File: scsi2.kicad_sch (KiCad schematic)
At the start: 0 parts

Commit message: Place CPLD, NCR and last 543 (Latched Trabceiver)
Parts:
- added U4: NCR53c710 SCSI Host Controller, Package_QFP:PQFP-160_28x28mm_P0.65mm, symbol NCRSCSI:NCR53c710

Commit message: Update design
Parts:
- added FB1: FerriteBead_Small, symbol Device:FerriteBead_Small
- added J3: TO-LED, Connector_PinHeader_2.54mm:PinHeader_1x03_P2.54mm_Vertical, symbol Connector:Conn_01x03_Pin
- added J4: TO-MB, Connector_PinHeader_2.54mm:PinHeader_1x03_P2.54mm_Vertical, symbol Connector:Conn_01x03_Pin
- added R1, R2, R3: 1K, symbol Device:R
- added R10, R6, R7, R8: 1K, YC324-FK-071KL:RESCAXS127P508X320X70-8N, symbol YC324-FK-071KL:YC324-FK-071KL
- added R11, R9: 120, Resistor_SMD:R_0603_1608Metric, symbol Device:R_Small
- added U7: SST39SF010, Package_SO:TSSOP-32_8x11mm_P0.65mm, symbol 39SF010-TSOP:SST39SF010
- added Y1: Abracon ACO-50MHz, Oscillator:Oscillator_DIP-14, symbol Oscillator:ACO-xxxMHz
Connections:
- net GND: now reaches U4.109 (V_{SS})
- net GND: now also U4.113 (V_{SS}), U4.118 (V_{SS}), U4.123 (V_{SS}), U4.128 (V_{SS}), U4.136 (V_{SS}), U4.143 (V_{SS}), U4.149 (V_{SS}), U4.15 (V_{SS}), U4.156 (V_{SS}), U4.2 (V_{SS}), U4.22 (V_{SS}), U4.31 (V_{SS}), U4.46 (V_{SS}), U4.54 (V_{SS}), U4.61 (V_{SS}), U4.69 (V_{SS}), U4.75 (V_{SS}), U4.82 (V_{SS}), U4.9 (V_{SS}), U4.96 (V_{SS}), U7.24 (GND), U7.30 (CE), Y1.7 (GND)
- net V5: now reaches U4.139 (V_{DD})
- net V5: now also U4.153 (V_{DD}), U4.19 (V_{DD}), U4.39 (V_{DD}), U4.40 (~{HALT}/~{TIP}), U4.49 (V_{DD}), U4.6 (V_{DD}), U4.64 (V_{DD}), U4.79 (V_{DD}), U4.90 (~{BIG_LIT}), U4.91 (BS), U4.95 (~{BOFF}), U4.99 (V_{DD}), J3.2 (Pin_2), J4.2 (Pin_2), R1.1, R10.5, R10.6, R10.7, R10.8, R2.1, R3.1, R6.5, R6.6, R6.7, R6.8, R7.6, R7.7, R7.8, R8.5, R8.6, R8.7, R8.8, U7.8 (VCC), Y1.14 (Vcc)
- net A14: now reaches U4.1 (A14)
- net A14: now also U7.12 (A12)
- net A20: now reaches U4.10 (A20)
- net A20: now also U7.9 (NC)
- net CLK_50M: now reaches U4.102 (SCLK)
- net CLK_50M: now also R11.2
- net NCR_INT: now reaches U4.105 (~{IRQ0})
- net A21: now reaches U4.11 (A21)
- net SCTRL_IO: now reaches U4.110 (I/O)
- net SCTRL_REQ: now reaches U4.111 (~{REQ})
- net SCTRL_CD: now reaches U4.112 (C/D)
- net SCTRL_SEL: now reaches U4.114 (~{SEL})
- net SCTRL_MSG: now reaches U4.115 (~{MSG})
- net SCTRL_RST: now reaches U4.116 (~{RST})
- net SCTRL_ACK: now reaches U4.117 (~{ACK})
- net SCTRL_BSY: now reaches U4.119 (~{BSY})
- net A22: now reaches U4.12 (A22)
- net SCTRL_ATN: now reaches U4.120 (~{ATN})
- net SCDATP: now reaches U4.121 (~{SDP})
- net SCDAT7: now reaches U4.122 (~{SD7})
- net SCDAT6: now reaches U4.124 (~{SD6})
- net SCDAT5: now reaches U4.125 (~{SD5})
- net SCDAT4: now reaches U4.126 (~{SD4})
- net SCDAT3: now reaches U4.127 (~{SD3})
- net SCDAT2: now reaches U4.129 (~{SD2})
- net A23: now reaches U4.13 (A23)
- net SCDAT1: now reaches U4.130 (~{SD1})
- net SCDAT0: now reaches U4.131 (~{SD0})
- net A24: now reaches U4.14 (A24)
- net A0: now reaches U4.144 (A0)
- net A0: now also R8.4
- net A1: now reaches U4.145 (A1)
- net A1: now also R8.3
- net A2: now reaches U4.146 (A2)
- net A2: now also R8.2, U7.20 (A0)
- net A3: now reaches U4.147 (A3)
- net A3: now also R8.1, U7.19 (A1)
- net A4: now reaches U4.148 (A4)
- net A4: now also U7.18 (A2)
- net A5: now reaches U4.150 (A5)
- net A5: now also U7.17 (A3)
- net A6: now reaches U4.151 (A6)
- net A6: now also U7.16 (A4)
- net A7: now reaches U4.152 (A7)
- net A7: now also U7.15 (A5)
- net A8: now reaches U4.154 (A8)
- net A8: now also U7.14 (A6)
- net A9: now reaches U4.155 (A9)
- net A9: now also U7.13 (A7)
- net A10: now reaches U4.157 (A10)
- net A10: now also U7.3 (A8)
- net A11: now reaches U4.158 (A11)
- net A11: now also U7.2 (A9)
- net A12: now reaches U4.159 (A12)
- net A12: now also U7.31 (A10)
- net A25: now reaches U4.16 (A25)
- net A13: now reaches U4.160 (A13)
- net A13: now also U7.1 (A11)
- net A26: now reaches U4.17 (A26)
- net A27: now reaches U4.18 (A27)
- net A28: now reaches U4.20 (A28)
- net A29: now reaches U4.21 (A29)
- net A30: now reaches U4.23 (A30)
- net A31: now reaches U4.24 (A31)
- net PLD_AS: now reaches U4.25 (~{AS}/~{TS})
- net PLD_AS: now also R7.3
- net PLD_SIZ1: now reaches U4.26 (SIZ1)
- net PLD_SIZ1: now also R7.2
- net PLD_SIZ0: now reaches U4.27 (SIZ0)
- net PLD_SIZ0: now also R7.1
- net PLD_FC2: now reaches U4.28 (FCS2/TM2)
- net PLD_FC1: now reaches U4.29 (FCS1/TM1)
- net A15: now reaches U4.3 (A15)
- net A15: now also U7.4 (A13)
- net PLD_FC0: now reaches U4.30 (FCS0/TM0)
- net PLD_READ: now reaches U4.32 (R_W)
- net CBREQ: now reaches U4.33 (~{CBREQ}/~{TT1})
- net CBREQ: now also R6.4
- net CBACK: now reaches U4.35 (~{CBACK}/~{TBI})
- net CBACK: now also R6.3
- net STERM: now reaches U4.36 (STERM/~{TA})
- net STERM: now also R6.2
- net BERR: now reaches U4.37 (~{BERR}/~{TEA})
- net BERR: now also R6.1
- net MASTER: now reaches U4.38 (~{MASTER})
- net A16: now reaches U4.4 (A16)
- net A16: now also U7.5 (A14)
- net CLK: now reaches U4.41 (BCLK)
- net D31: now reaches U4.42 (D31)
- net D31: now also U7.29 (D7)
- net D30: now reaches U4.43 (D30)
- net D30: now also U7.28 (D6)
- net D29: now reaches U4.44 (D29)
- net D29: now also U7.27 (D5)
- net D28: now reaches U4.45 (D28)
- net D28: now also U7.26 (D4)
- net D27: now reaches U4.47 (D27)
- net D26: now reaches U4.48 (D26)
- net A17: now reaches U4.5 (A17)
- net A17: now also U7.11 (A15)
- net D25: now reaches U4.50 (D25)
- net D24: now reaches U4.51 (D24)
- net DP3_ABRT: now reaches U4.52 (DP3/~{ABRT})
- net DP3_ABRT: now also R10.1
- net D23: now reaches U4.53 (D23)
- net D22: now reaches U4.55 (D22)
- net D21: now reaches U4.56 (D21)
- net D20: now reaches U4.57 (D20)
- net D19: now reaches U4.58 (D19)
- net D18: now reaches U4.59 (D18)
- net D17: now reaches U4.60 (D17)
- net D16: now reaches U4.62 (D16)
- net at U4.63 (DP2): now also R3.2
- net D15: now reaches U4.65 (D15)
- net D15: now also U7.25 (D3)
- net D14: now reaches U4.66 (D14)
- net D14: now also U7.23 (D2)
- net D13: now reaches U4.67 (D13)
- net D13: now also U7.22 (D1)
- net D12: now reaches U4.68 (D12)
- net D12: now also U7.21 (D0)
- net A18: now reaches U4.7 (A18)
- net A18: now also U7.10 (A16)
- net D11: now reaches U4.70 (D11)
- net D10: now reaches U4.71 (D10)
- net D9: now reaches U4.72 (D9)
- net D8: now reaches U4.73 (D8)
- net at U4.74 (DP1): now also R2.2
- net D7: now reaches U4.76 (D7)
- net D6: now reaches U4.77 (D6)
- net D5: now reaches U4.78 (D5)
- net A19: now reaches U4.8 (A19)
- net A19: now also U7.6 (NC)
- net D4: now reaches U4.80 (D4)
- net D3: now reaches U4.81 (D3)
- net D2: now reaches U4.83 (D2)
- net D1: now reaches U4.84 (D1)
- net D0: now reaches U4.85 (D0)
- net at U4.86 (DP0): now also R1.2
- net PLD_DS: now reaches U4.87 (~{DS}/DLE)
- net PLD_DS: now also R10.2
- net SLACK: now reaches U4.92 (~{SLACK})
- net SREG: now reaches U4.93 (~{CS})
- new net: R11.1, Y1.8 (OUT)
- new net BGACK: R10.4
- new net IORST: R10.3
- new net LED: R9.1
- new net LEDR: J3.1 (Pin_1), J3.3 (Pin_3), J4.1 (Pin_1), J4.3 (Pin_3), R9.2
- new net ROM_OE: U7.32 (OE)
- new net ROM_WE: U7.7 (PGM)
- no-connect marks 0 -> 18

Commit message: More work. Getting there.
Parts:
- removed R1, R2, R3: 1K, symbol Device:R
- added C34, C36, C38, C40, C42: 0.1uF, symbol Device:C_Small
- added C35, C37, C39, C41: 10uF, symbol Device:C_Small
- added R17: 1K, YC324-FK-071KL:RESCAXS127P508X320X70-8N, symbol YC324-FK-071KL:YC324-FK-071KL
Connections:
- net BGACK: now also R10.3; no longer R10.4
- net DP3_ABRT: now also R17.4; no longer R10.1
- net GND: now also C34.2, C35.2, C36.2, C37.2, C38.2, C39.2, C40.2, C41.2, C42.2
- net IORST: now also R10.2; no longer R10.3
- net PLD_DS: now also R10.1; no longer R10.2
- net SLACK: now also U4.94 (~{RESET}); no longer U4.92 (~{SLACK})
- net SREG: now also U4.95 (~{BOFF}); no longer U4.93 (~{CS})
- net V5: now also U4.92 (~{SLACK}), U4.93 (~{CS}), U4.97 (~{FETCH}), C34.1, C35.1, C36.1, C37.1, C38.1, C39.1, C40.1, C41.1, C42.1, R17.5, R17.6, R17.7, R17.8; no longer R10.5, U4.90 (~{BIG_LIT}), U4.91 (BS), U4.95 (~{BOFF})
- net DP1: now reaches U4.74 (DP1)
- net DP1: now also R17.2
- net DP0: now reaches U4.86 (DP0)
- net DP0: now also R17.1
- net DP2: now reaches U4.63 (DP2)
- net DP2: now also R17.3
- no-connect marks 18 -> 22
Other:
- note added: "P136 <-> P139"
- note added: "P15 <-> P19"
- note added: "P153 <-> P156"
- note added: "P2 <-> P6"
- note added: "P31 <-> P39"
- note added: "P49 <-> P54"
- note added: "P64 <-> P69"
- note added: "P75 <-> P79"
- note added: "P96 <-> P99"
- moved on the sheet: FB1, J3, J4, R10, R6, R7, R8, R9, U7

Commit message: Latest updates
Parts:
- added C32: 10nF, Capacitor_SMD:C_0603_1608Metric_Pad1.08x0.95mm_HandSolder, symbol Device:C_Small
- added FB2, FB3: 60, Capacitor_SMD:C_0603_1608Metric_Pad1.08x0.95mm_HandSolder, symbol Device:FerriteBead_Small
- added R1, R2: 22, Resistor_SMD:R_0603_1608Metric_Pad0.98x0.95mm_HandSolder, symbol Device:R_Small
- added U15: 74ABT74, Package_SO:TSSOP-14_4.4x5mm_P0.65mm, symbol NCRSCSI:74ABT74
- C34, C36, C38, C40, C42: value 0.1uF -> 100nF; footprint (none) -> Capacitor_SMD:C_0603_1608Metric_Pad1.08x0.95mm_HandSolder
- C35, C37, C39, C41: value 10uF -> 10nF; footprint (none) -> Capacitor_SMD:C_0603_1608Metric_Pad1.08x0.95mm_HandSolder
- FB1: value FerriteBead_Small -> 60; footprint (none) -> Capacitor_SMD:C_0603_1608Metric_Pad1.08x0.95mm_HandSolder
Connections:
- net BGACK: now also U4.98 (~{BGACK}/~{BB})
- net CLK: now also R2.1
- net CLK_50M: now also U15.3 (C)
- net GND: now also C32.1, U15.7 (GND)
- net IORST: now also U4.94 (~{RESET})
- net MASTER: now also FB3.2; no longer U4.38 (~{MASTER})
- net PLD_READ: now also FB2.2; no longer U4.32 (R_W)
- net SLACK: now also U4.92 (~{SLACK}); no longer U4.94 (~{RESET})
- net SREG: now also U4.93 (~{CS}); no longer U4.95 (~{BOFF})
- net V5: now also U4.90 (~{BIG_LIT}), U4.91 (BS), U4.95 (~{BOFF}), C32.2, U15.1 (~{R}), U15.10 (~{S}), U15.11 (C), U15.12 (D), U15.13 (~{R}), U15.14 (VCC), U15.4 (~{S}); no longer U4.92 (~{SLACK}), U4.93 (~{CS})
- net at FB1.1: now also U4.101 (~{BR})
- net SBR: now reaches FB1.2
- net SBG: now reaches U4.100 (~{BG})
- new net: R2.2, U15.5 (Q)
- new net: R1.2, U15.6 (~{Q})
- new net: FB2.1, U4.32 (R_W)
- new net: FB3.1, U4.38 (~{MASTER})
- new net CLKI: R1.1, U15.2 (D)
- no-connect marks 22 -> 23
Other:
- moved on the sheet: FB1, R11, Y1

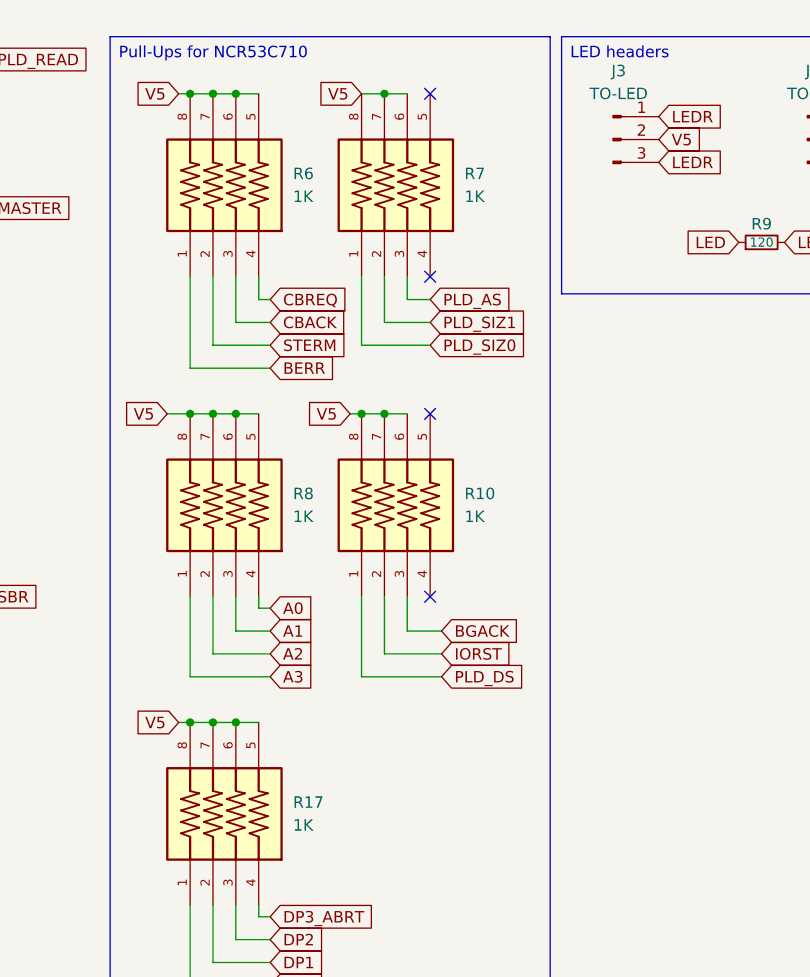
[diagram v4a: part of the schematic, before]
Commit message: Update RN footprint to CAY16_102J4LF
- Rename RNs from R to RN.
- Fix U5 footprint
- Rename pages to be consecutive numbers
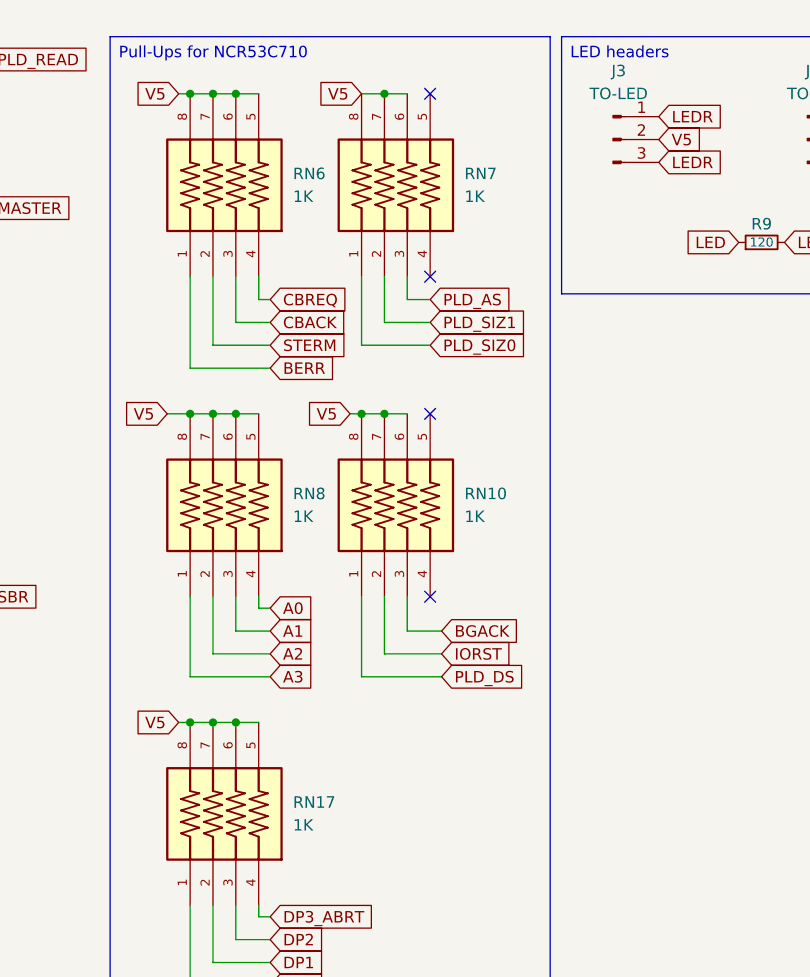
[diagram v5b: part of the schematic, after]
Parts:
- RN10: renamed from R10; footprint YC324-FK-071KL:RESCAXS127P508X320X70-8N -> CAY16_102J4LF:BO_CAY16
- RN17: renamed from R17; footprint YC324-FK-071KL:RESCAXS127P508X320X70-8N -> CAY16_102J4LF:BO_CAY16
- RN6: renamed from R6; footprint YC324-FK-071KL:RESCAXS127P508X320X70-8N -> CAY16_102J4LF:BO_CAY16
- RN7: renamed from R7; footprint YC324-FK-071KL:RESCAXS127P508X320X70-8N -> CAY16_102J4LF:BO_CAY16
- RN8: renamed from R8; footprint YC324-FK-071KL:RESCAXS127P508X320X70-8N -> CAY16_102J4LF:BO_CAY16
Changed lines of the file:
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@@
 		(dnp no)
 		(fields_autoplaced yes)
-		(property "Reference" "R6"
+		(property "Reference" "RN6"
 			(at 135.89 101.5999 90)
 			(effects
@@
 			)
 		)
-		(property "Footprint" "YC324-FK-071KL:RESCAXS127P508X320X70-8N"
+		(property "Footprint" "CAY16_102J4LF:BO_CAY16"
 			(at 129.54 102.87 0)
 			(effects
@@
 			(project ""
 				(path "/8f9f4021-47aa-41d9-bea7-f6ccf72098bb/2daf4fe3-1e72-4ad5-914a-264df02f69b3"
-					(reference "R6")
+					(reference "RN6")
 					(unit 1)
 				)
@@
 		(dnp no)
 		(fields_autoplaced yes)
-		(property "Reference" "R10"
+		(property "Reference" "RN10"
 			(at 154.94 137.1599 90)
 			(effects
@@
 			)
 		)
-		(property "Footprint" "YC324-FK-071KL:RESCAXS127P508X320X70-8N"
+		(property "Footprint" "CAY16_102J4LF:BO_CAY16"
 			(at 148.59 138.43 0)
 			(effects
@@
 			(project ""
 				(path "/8f9f4021-47aa-41d9-bea7-f6ccf72098bb/2daf4fe3-1e72-4ad5-914a-264df02f69b3"
-					(reference "R10")
+					(reference "RN10")
 					(unit 1)
 				)
@@
 		(dnp no)
 		(fields_autoplaced yes)
-		(property "Reference" "R7"
+		(property "Reference" "RN7"
 			(at 154.94 101.5999 90)
 			(effects
@@
 			)
 		)
-		(property "Footprint" "YC324-FK-071KL:RESCAXS127P508X320X70-8N"
+		(property "Footprint" "CAY16_102J4LF:BO_CAY16"
 			(at 148.59 102.87 0)
 			(effects
@@
 			(project ""
 				(path "/8f9f4021-47aa-41d9-bea7-f6ccf72098bb/2daf4fe3-1e72-4ad5-914a-264df02f69b3"
-					(reference "R7")
+					(reference "RN7")
 					(unit 1)
 				)
@@
 		(dnp no)
 		(fields_autoplaced yes)
-		(property "Reference" "R8"
+		(property "Reference" "RN8"
 			(at 135.89 137.1599 90)
 			(effects
@@
 			)
 		)
-		(property "Footprint" "YC324-FK-071KL:RESCAXS127P508X320X70-8N"
+		(property "Footprint" "CAY16_102J4LF:BO_CAY16"
 			(at 129.54 138.43 0)
 			(effects
@@
 			(project ""
 				(path "/8f9f4021-47aa-41d9-bea7-f6ccf72098bb/2daf4fe3-1e72-4ad5-914a-264df02f69b3"
-					(reference "R8")
+					(reference "RN8")
 					(unit 1)
 				)
@@
 		(dnp no)
 		(fields_autoplaced yes)
-		(property "Reference" "R17"
+		(property "Reference" "RN17"
 			(at 135.89 171.4499 90)
 			(effects
@@
 			)
 		)
-		(property "Footprint" "YC324-FK-071KL:RESCAXS127P508X320X70-8N"
+		(property "Footprint" "CAY16_102J4LF:BO_CAY16"
 			(at 129.54 172.72 0)
 			(effects
@@
 			(project "A4092"
 				(path "/8f9f4021-47aa-41d9-bea7-f6ccf72098bb/2daf4fe3-1e72-4ad5-914a-264df02f69b3"
-					(reference "R17")
-					(unit 1)
-				)
+					(reference "RN17")
+					(unit 1)
+				)

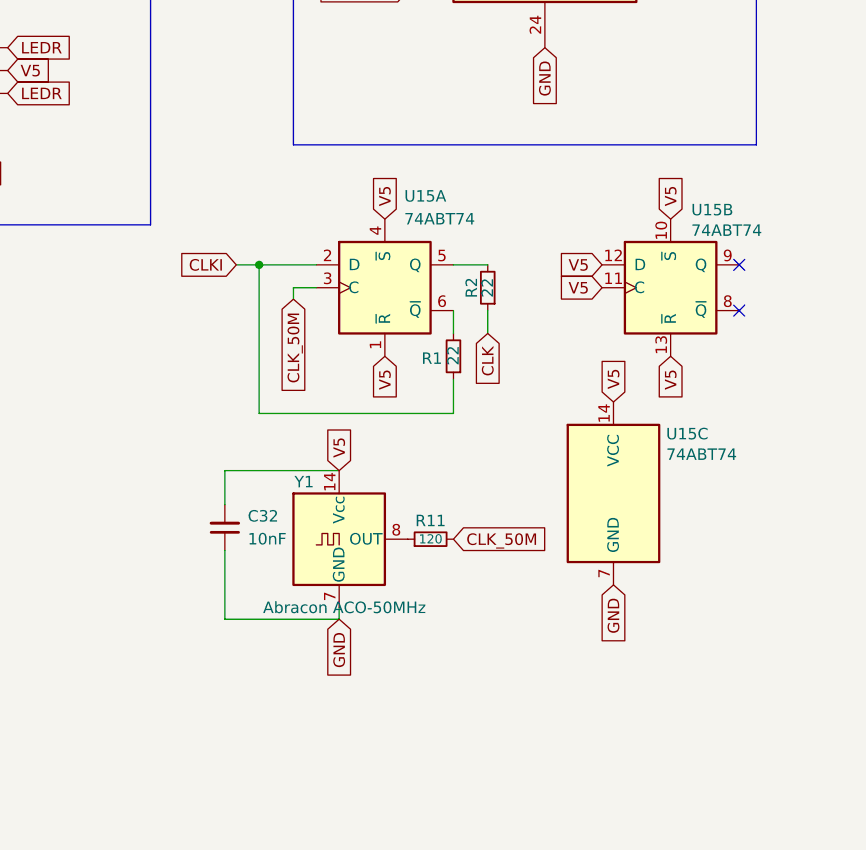
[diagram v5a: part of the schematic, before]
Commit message: Drop 74ABT74
The 74ABT74 is only used as a divider to create 25MHz from the 50MHz clock, and
it can be removed. Instead, the 50MHz are directly brought to the ATF1508. CLK
will be used as an output, not an input, so move away from GCLK pin. CLKI is no
longer needed on a pin as it doesn't connect to anything anymore.
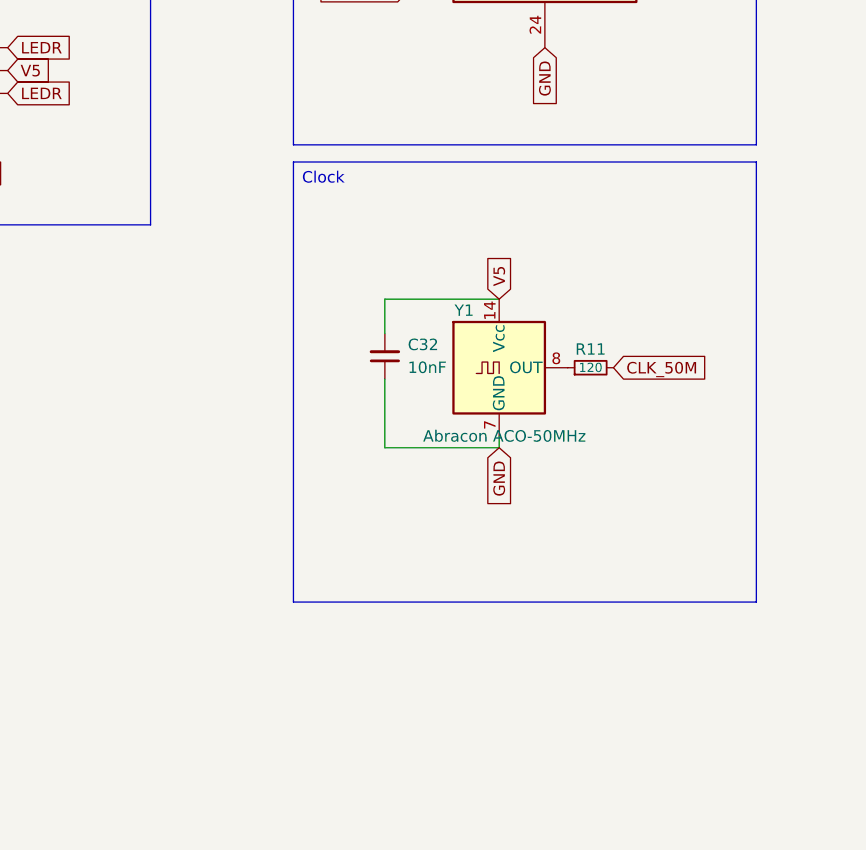
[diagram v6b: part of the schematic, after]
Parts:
- removed R1, R2: 22, Resistor_SMD:R_0603_1608Metric_Pad0.98x0.95mm_HandSolder, symbol Device:R_Small
- removed U15: 74ABT74, Package_SO:TSSOP-14_4.4x5mm_P0.65mm, symbol NCRSCSI:74ABT74
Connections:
- no-connect marks 23 -> 21
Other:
- moved on the sheet: C32, R11, Y1
